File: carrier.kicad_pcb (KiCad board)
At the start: 4 copper layers, 20.3 x 68.6 mm, 30 parts, among them J1 Conn_02x06_Odd_Even, J2 Conn_01x26, J3 Conn_01x26, U1 CARAVEL, U2 W25Q128JVS, U3 LP5907MFX-3.3, U4 LP5907MFX-1.8, U5 LP5907MFX-1.8, U6 LP5907MFX-3.3, X1 SG-5032CAN

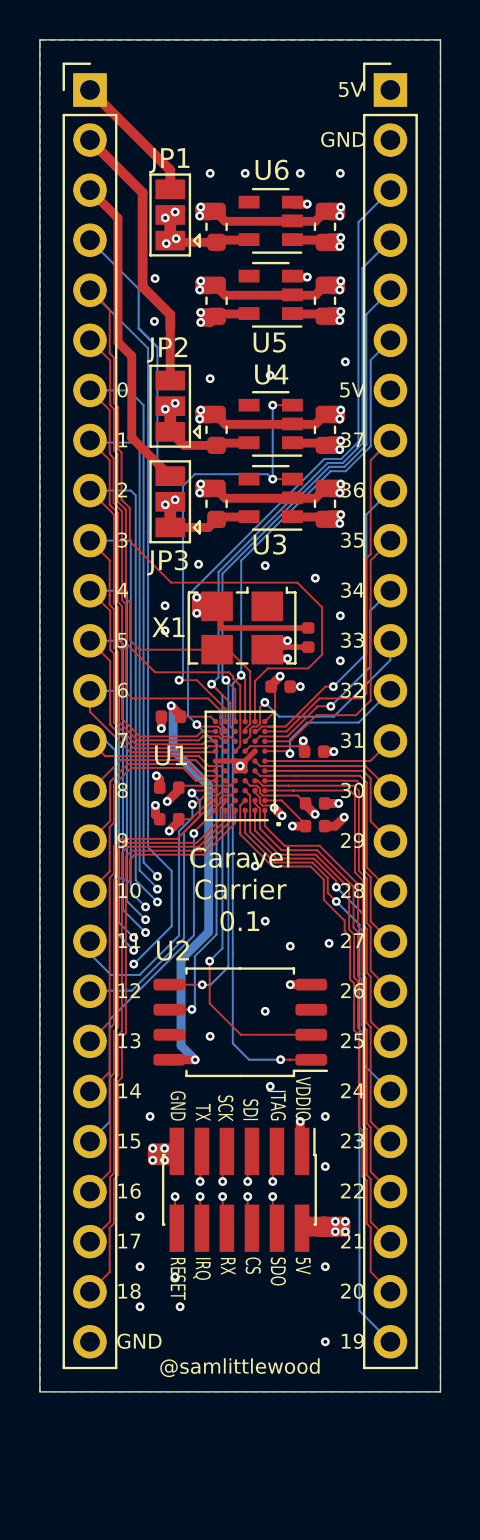
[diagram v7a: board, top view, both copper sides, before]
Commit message: Clean up clearances.
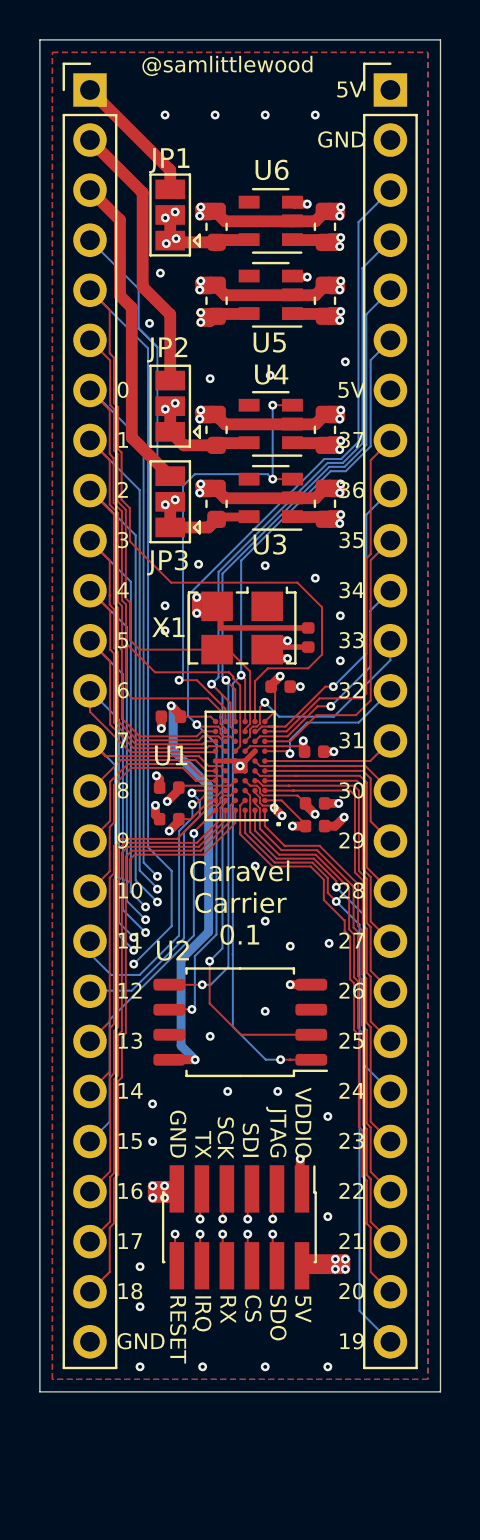
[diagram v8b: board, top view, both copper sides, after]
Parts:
- moved J1 1.91 mm to (68.7, 103.4)
- moved G*** 0.59 mm to (68.7, 101.0)
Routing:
- net vddio: track 55.9 -> 57.8 mm
- net mprj_io[7]: track 35.4 -> 36.9 mm
- net resetb: track 85.4 -> 86.5 mm
- net mprj_io[6]: track 37.9 -> 39.0 mm
- net mprj_io[5]: track 44.7 -> 45.7 mm
- net mprj_io[4]: track 48.3 -> 49.2 mm
- net mprj_io[32]: track 8.92 -> 8.15 mm
- net mprj_io[0]: track 70.6 -> 71.3 mm
- net mprj_io[2]: track 58.7 -> 59.4 mm
- net mprj_io[3]: track 55.3 -> 56.0 mm
- net ext_vddio: track 7.38 -> 6.73 mm
- net mprj_io[11]: track 15.3 -> 14.7 mm
- net GND: vias 66 -> 67
